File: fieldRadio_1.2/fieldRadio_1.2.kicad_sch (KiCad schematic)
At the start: 11 parts, among them J1 Conn_01x02, J12 AudioJack3_Switch, J18 Conn_01x16, J2 Conn_01x02, J3 Conn_01x03, J4 AudioJack2_Switch, J5 AudioJack3_Switch, J7 Conn_01x04, J8 Conn_01x12

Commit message: updating schematics for fieldRadio_1.2
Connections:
- net LPF/antenna renamed LPF/lpIn
- no-connect marks 13 -> 9
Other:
- removed sheet Preselector
- sheet LPF ports: added VDD5, hpIn, hpOut, lpIn, lpOut, registerClock, serialData, shiftClock; removed 15M, 17M, 20M, 30M, 40M, antenna, trswitch
- sheet controller ports: added BTN_BIN_MON, VDD_AMP_ENABLE, VDD_DRV_ENABLE, regClk, sel_binaural, serData, shiftClk, ~{RF_ENABLE}; removed BAND_15M, BAND_17M, BAND_20M, BAND_30M, BAND_40M, P1.4, P3.0, P5.6, SIDEBAND_SEL
- sheet powerAmp ports: added VDD_AMP_ENABLE, VDD_DRV_ENABLE, ~{RF_ENABLE}; removed VDD_AMP_enable, bst_enable, vdrv_enable, ~{rf_enable}
- sheet qsd ports: added iclk, qclk; removed SIDEBAND_SEL, rfClock

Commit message: Working on fieldRadio_1.2 schematics
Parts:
- removed J8: Conn_01x12, Connector_PinHeader_2.54mm:PinHeader_1x12_P2.54mm_Vertical, symbol Connector_Generic:Conn_01x12
- added J14, J8: Conn_01x02, Connector_PinHeader_2.54mm:PinHeader_1x02_P2.54mm_Vertical, symbol Connector_Generic:Conn_01x02
- added J6: Conn_01x10, symbol Connector_Generic:Conn_01x10
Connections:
- net GND: now also J14.2 (Pin_2), J6.10 (Pin_10), J6.2 (Pin_2), J6.6 (Pin_6)
- net TX_LED: now also J8.1 (Pin_1)
- net VDD5: now also J6.1 (Pin_1), J8.2 (Pin_2); no longer C1.1, C2.1
- new net: C1.1, C2.1
- new net BTN_ENCODER_A: J6.7 (Pin_7)
- new net BTN_ENCODER_B: J6.8 (Pin_8)
- new net BTN_ENCODER_SW: J6.9 (Pin_9)
- new net REG_CLK: J6.5 (Pin_5)
- new net SERIAL_CLK: J6.4 (Pin_4)
- new net SERIAL_DATA: J6.3 (Pin_3)
- new net controller/BTN_TXMODE: J14.1 (Pin_1)
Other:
- sheet LPF ports: added SERIAL_OUT; removed VDD5
- sheet controller ports: added BTN_ENCODER_A, BTN_ENCODER_B, BTN_ENCODER_SW, REG_CLK, SERIAL_CLK, SERIAL_DATA; removed BTN_BAND_SEL, BTN_BIN_MON, BTN_DIGIT_SEL, BTN_FILTER_SEL, BTN_MENU, BTN_MODE, BTN_MUTE, BTN_NOT_USED, BTN_SPOT, regClk, serData, shiftClk
- note added: "to TX enable btn"
- note added: "to TX led"
- moved on the sheet: C1, C2, J18, J7

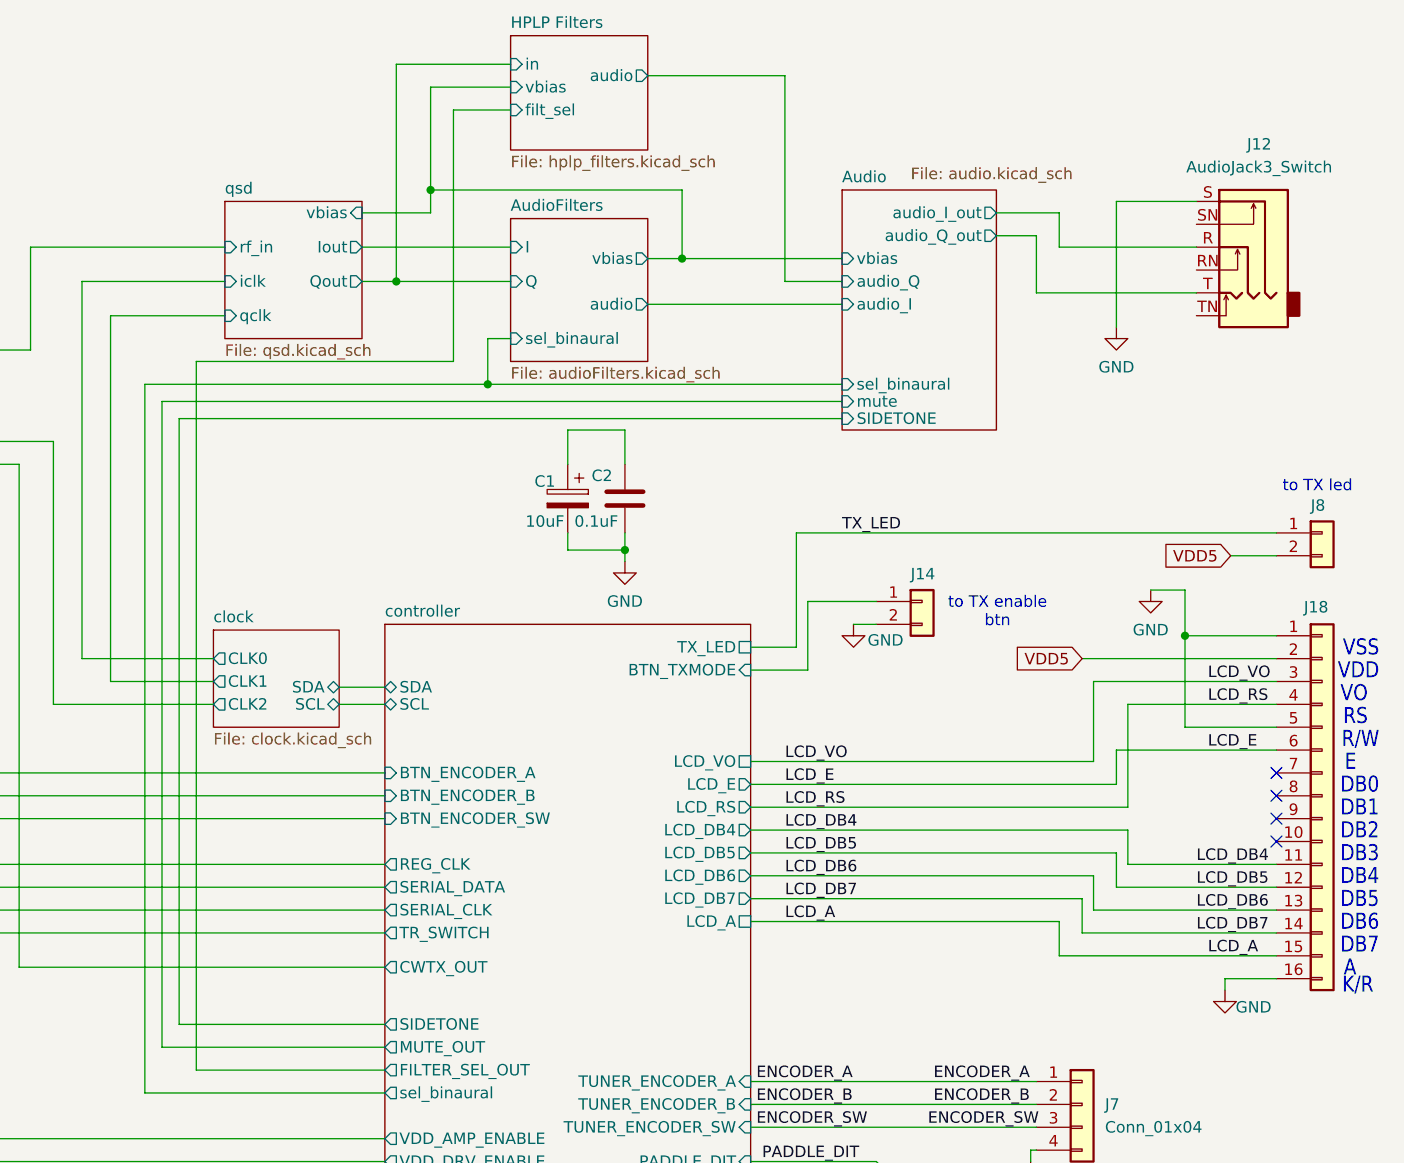
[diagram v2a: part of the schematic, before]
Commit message: adding jlcpcb part numbers to schematics
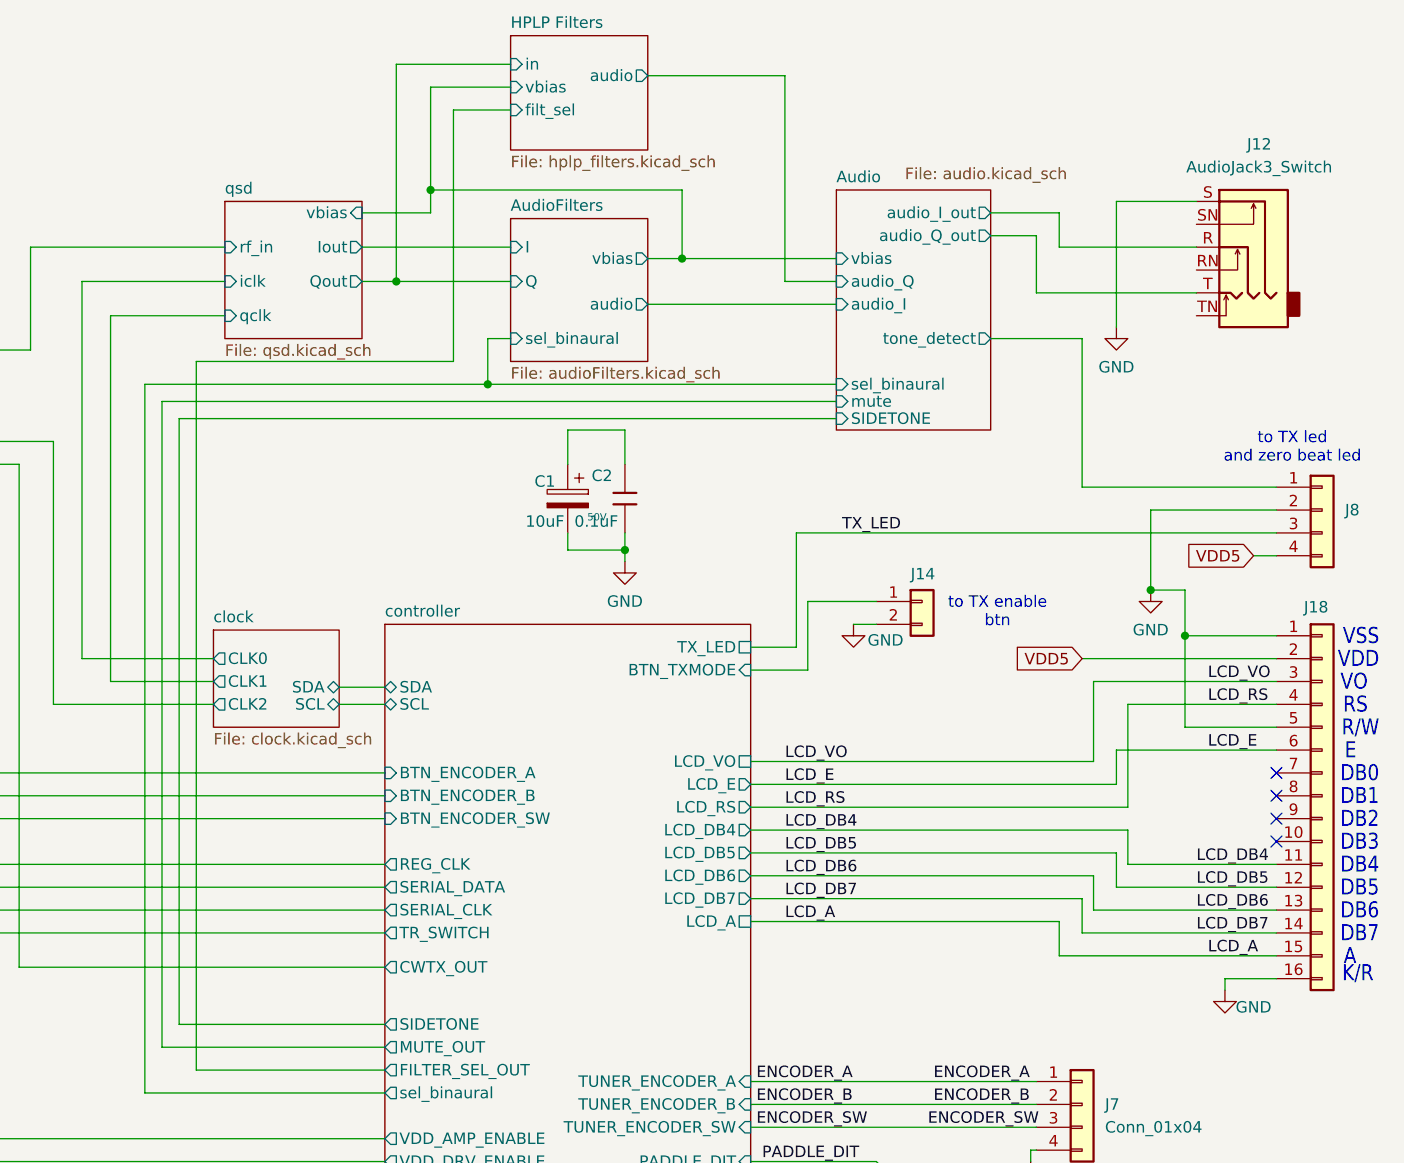
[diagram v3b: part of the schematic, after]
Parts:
- removed J8: Conn_01x02, Connector_PinHeader_2.54mm:PinHeader_1x02_P2.54mm_Vertical, symbol Connector_Generic:Conn_01x02
- added J8: Conn_01x04, Connector_PinHeader_2.54mm:PinHeader_1x04_P2.54mm_Vertical, symbol Connector_Generic:Conn_01x04
- C2: footprint Capacitor_SMD:C_0603_1608Metric_Pad1.08x0.95mm_HandSolder -> PCM_JLCPCB:C_0603; symbol Device:C -> PCM_JLCPCB-Capacitors:0603,100nF; Attrition Qty (none) -> 10; Capacitance (none) -> 100nF; Category (none) -> Capacitors,Multilayer Ceramic Capacitors MLCC - SMD/SMT; Class (none) -> Basic Component; LCSC (none) -> C14663; Manufacturer (none) -> YAGEO; Minimum Qty (none) -> 20; Part (none) -> CC0603KRX7R9BB104; Price (none) -> 0.006USD; Process (none) -> SMT; Stock (none) -> 70324515; Temperature Coefficient (none) -> X7R; Tolerance (none) -> ±10%; Voltage Rated (none) -> 50V
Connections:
- net GND: now also J8.2 (Pin_2)
- net TX_LED: now also J8.3 (Pin_3)
- net VDD5: now also J8.4 (Pin_4)
- new net Audio/tone_detect: J8.1 (Pin_1)
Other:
- sheet Audio ports: added tone_detect; removed none
- note added: "to TX led and zero beat led"
- note removed: "to TX led"

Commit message: continued symbol property updates
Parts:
- removed C1: 10uF, Capacitor_THT:CP_Radial_D5.0mm_P2.00mm, symbol Device:C_Polarized
- removed C2: 0.1uF, PCM_JLCPCB:C_0603, symbol PCM_JLCPCB-Capacitors:0603,100nF
- J1, J12, J14, J18, J2, J3, J4, J5, J6, J7, J8: now left out of the parts list
